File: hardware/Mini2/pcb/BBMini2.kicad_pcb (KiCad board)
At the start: 4 copper layers, 89 x 48 mm, 75 parts, among them J1 Barrel_Jack_Switch, J2 USB_B_Mini, J3 Display, Q1 MBT2222ADW1T1, SW1 SW_SPDT, SW2 SW_Push, SW3 SW_Push, SW4 SW_Push, U1 ESP8266EX, U2 AT25SF081-SSHF-X, U3 AP2112K-3.3, U4 CP2104, U5 MCP3208, U6 LM2576S-5, Y1 ABM8-26.000MHZ-10-1-U-T

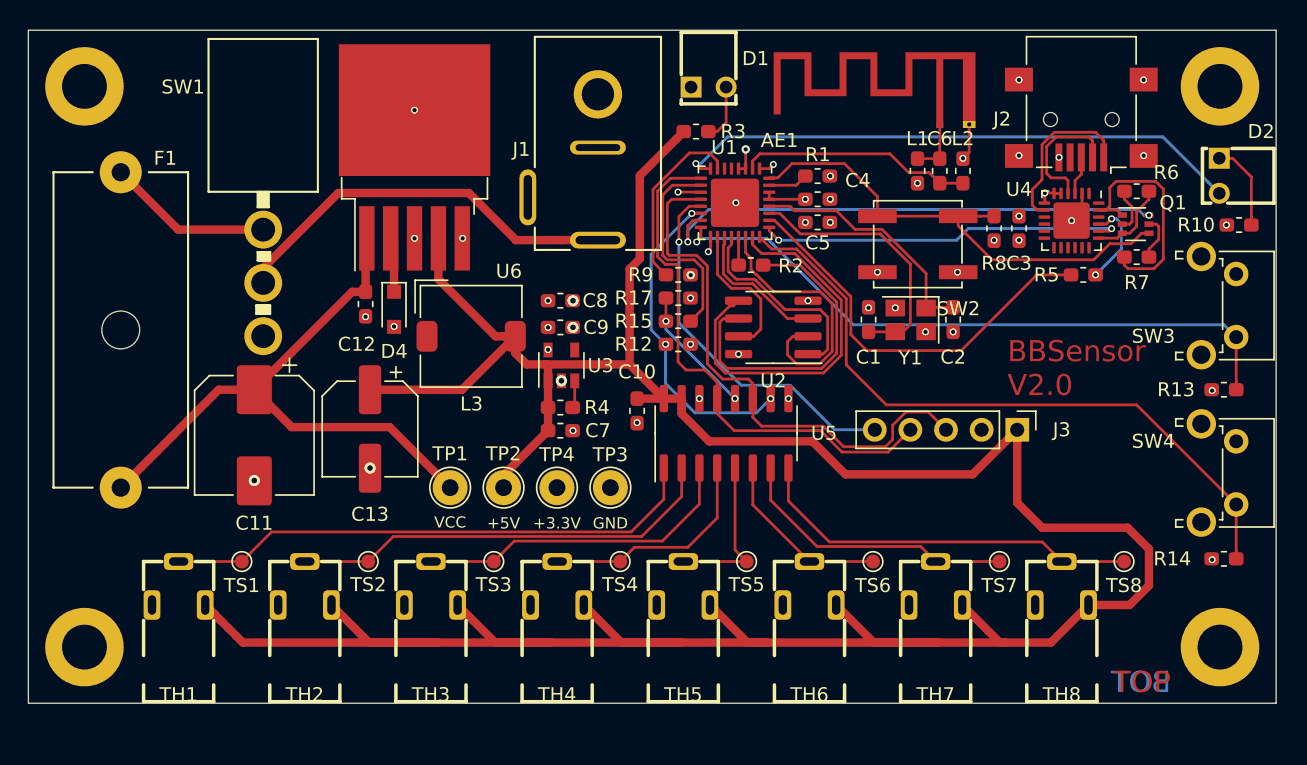
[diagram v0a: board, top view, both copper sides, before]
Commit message: feat: BBMini2 - experimental ESP8266 PCB (SMD)
* shrink pcb, add cad

Issue #23
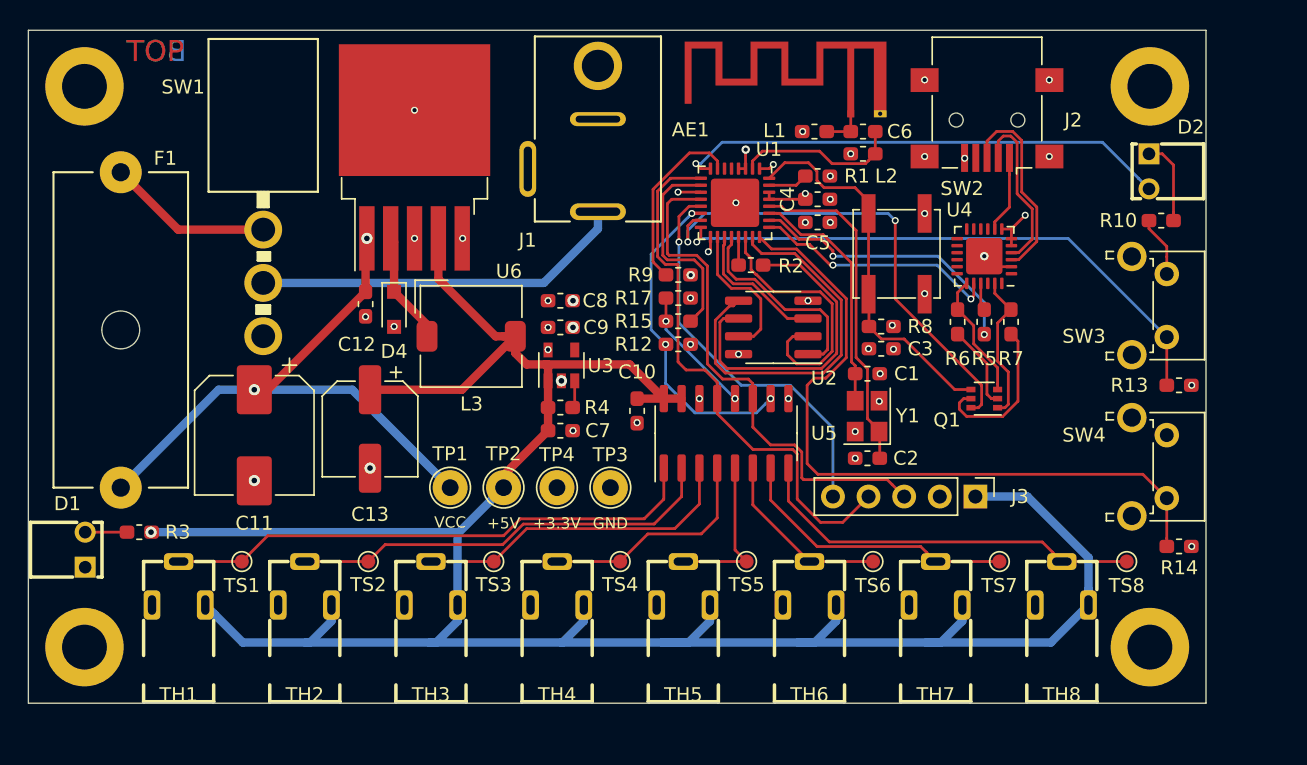
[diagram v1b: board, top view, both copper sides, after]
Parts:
- J1: footprint Collection:CLIFF_DC_SOCKET_2.5 -> Collection:CLIFF_DC_SOCKET_2.5_Short
- moved D1 61.0 mm to (15.1, 52.0), turned to 90 degrees
- moved R3 48.9 mm to (22.9, 50.8), turned to 0 degrees
- moved Q1 16.5 mm to (83.2, 41.3), turned to 180 degrees
- moved R6 15.8 mm to (81.3, 35.8), turned to 270 degrees
- moved C3 13.1 mm to (75.8, 37.7), turned to 180 degrees
- moved C2 11.6 mm to (74.9, 45.5), turned to 0 degrees
- moved R8 10.7 mm to (75.8, 36.1), turned to 0 degrees
- moved R7 10.1 mm to (85.1, 35.8), turned to 270 degrees
- moved L1 7.87 mm to (71.1, 22.2), turned to 180 degrees
- moved R5 7.82 mm to (83.2, 35.8), turned to 270 degrees
- moved Y1 7.53 mm to (74.8, 42.5), turned to 90 degrees
- moved L2 7.23 mm to (74.5, 23.8), turned to 180 degrees
- moved J2 6.73 mm to (83.4, 21.4)
- moved U4 6.72 mm to (83.2, 31.1), turned to 180 degrees
- moved AE1 6.40 mm to (73.7, 21.0)
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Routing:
- net +5V: track 225.8 -> 183.6 mm, vias 0 -> 1
- net Net-(J2-Pad3): track 2.76 -> 14.2 mm
- net /ESP8266EX/GPIO3_RXD: track 29.2 -> 20.3 mm, vias 0 -> 2
- net /ESP8266EX/GPIO1_TXD: track 26.3 -> 17.7 mm
- net Net-(Q1-Pad5): track 3.24 -> 11.2 mm
- net /ESP8266EX/~RST: track 34.9 -> 27.2 mm
- net /Serial/DTR: track 17.0 -> 10.7 mm
- net Net-(J2-Pad1): track 11.8 -> 5.51 mm
- net /ESP8266EX/XTAL_IN: track 17.6 -> 23.9 mm
- net +3V3: track 10.7 -> 16.6 mm, vias 16 -> 15
- net /ESP8266EX/GPIO16: track 41.0 -> 35.5 mm
- net /ESP8266EX/GPIO4: track 46.4 -> 41.1 mm
- net /ESP8266EX/LNA: track 16.6 -> 11.8 mm
- net /Serial/USB_RX: track 6.34 -> 1.98 mm, vias 2 -> 0
- net Net-(D4-Pad1): track 3.91 -> 8.06 mm
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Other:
- board size 89 x 48 mm -> 84 x 48 mm
- board text removed: "BBSensor V2.0"

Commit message: feat: BBMini2 - experimental ESP8266 PCB (SMD)
* redo PCB, add CAD
* make space for Display

Issue #23
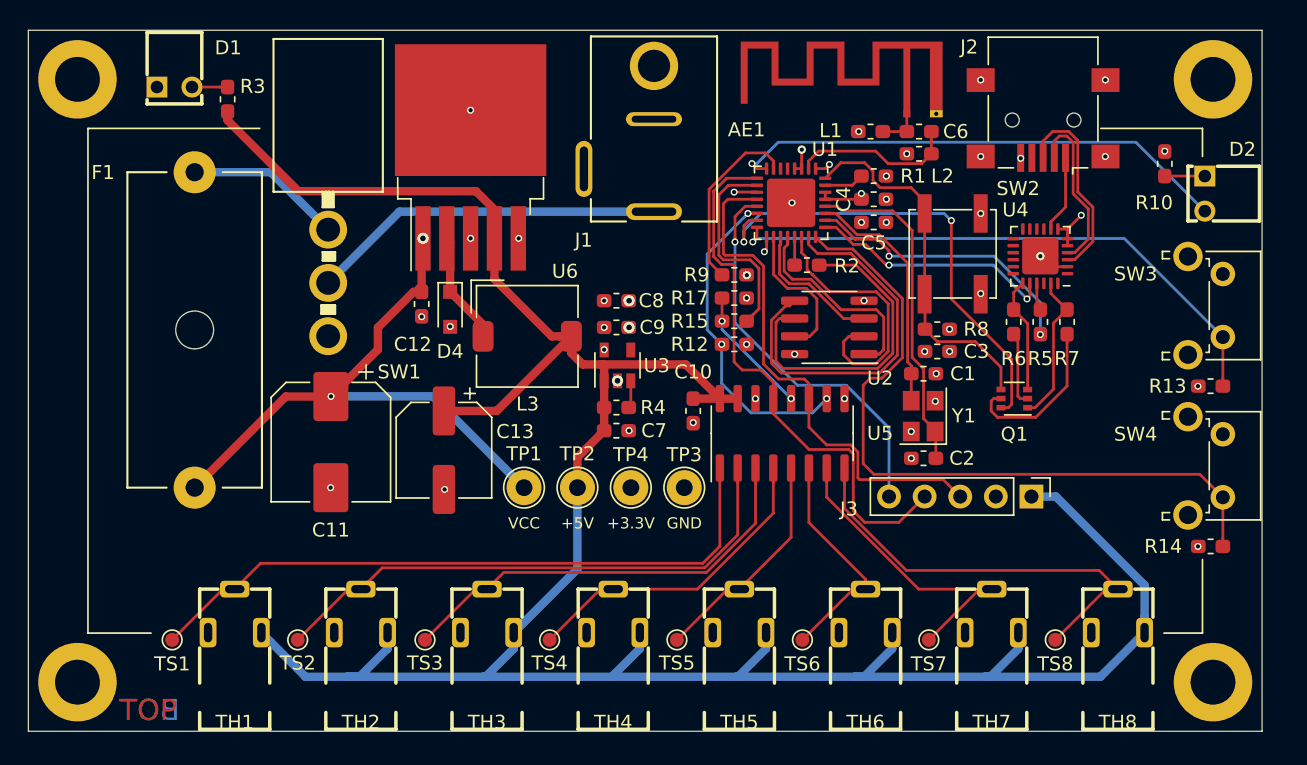
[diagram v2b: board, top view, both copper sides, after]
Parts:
- removed the ~ at (95.0, 19.0)
- removed the ~ at (19.0, 19.0)
- added ~: MountingHole_3.2mm_M3_DIN965_Pad, MountingHole:MountingHole_3.2mm_M3_DIN965_Pad, F.Cu at (18.5, 18.5)
- added ~: MountingHole_3.2mm_M3_DIN965_Pad, MountingHole:MountingHole_3.2mm_M3_DIN965_Pad, F.Cu at (99.5, 18.5)
- moved D1 38.4 mm to (25.4, 15.1), turned to 0 degrees
- moved R3 31.5 mm to (29.2, 19.9), turned to 270 degrees
- moved TS8 7.56 mm to (88.2, 58.5)
- moved TS2 7.52 mm to (34.2, 58.5)
- moved TS4 7.52 mm to (52.2, 58.5)
- moved TS6 7.52 mm to (70.2, 58.5)
- moved TS7 7.52 mm to (79.2, 58.5)
- moved TS5 7.48 mm to (61.3, 58.5)
- moved TS1 7.48 mm to (25.3, 58.5)
- moved TS3 7.44 mm to (43.3, 58.5)
- moved C13 5.48 mm to (44.6, 45.0)
- moved C11 5.48 mm to (36.6, 44.4)
- moved TP4 5.27 mm to (58.0, 47.6)
- moved F1 5.27 mm to (26.9, 47.6)
- moved TP1 5.27 mm to (50.4, 47.6)
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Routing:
- net /Temperature/SIGNAL1: track 38.7 -> 47.4 mm
- net /Temperature/SIGNAL2: track 30.8 -> 39.3 mm
- net /Temperature/SIGNAL3: track 23.4 -> 31.0 mm
- net /Temperature/SIGNAL4: track 16.3 -> 22.9 mm
- net +5V: track 183.6 -> 189.7 mm, vias 1 -> 0
- net /Temperature/SIGNAL5: track 11.5 -> 16.1 mm
- net +3V3: track 16.6 -> 12.2 mm, vias 15 -> 16
- net /Temperature/SIGNAL6: track 12.9 -> 16.3 mm
- net Net-(D2-Pad1): track 6.04 -> 2.86 mm
- net /Temperature/SIGNAL8: track 28.5 -> 30.7 mm
- net /Temperature/SIGNAL7: track 20.4 -> 22.6 mm
- net Net-(J1-Pad1): track 26.7 -> 25.3 mm
- net /ESP8266EX/~RST: track 27.2 -> 26.3 mm
- net /Serial/RTS: track 9.03 -> 8.26 mm
- net /ESP8266EX/GPIO0: track 35.1 -> 34.3 mm
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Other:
- board size 84 x 48 mm -> 88 x 50 mm

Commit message: feat: BBMini2 - experimental ESP8266 PCB (SMD)
* finalize new Case (experimental)

Issue #23
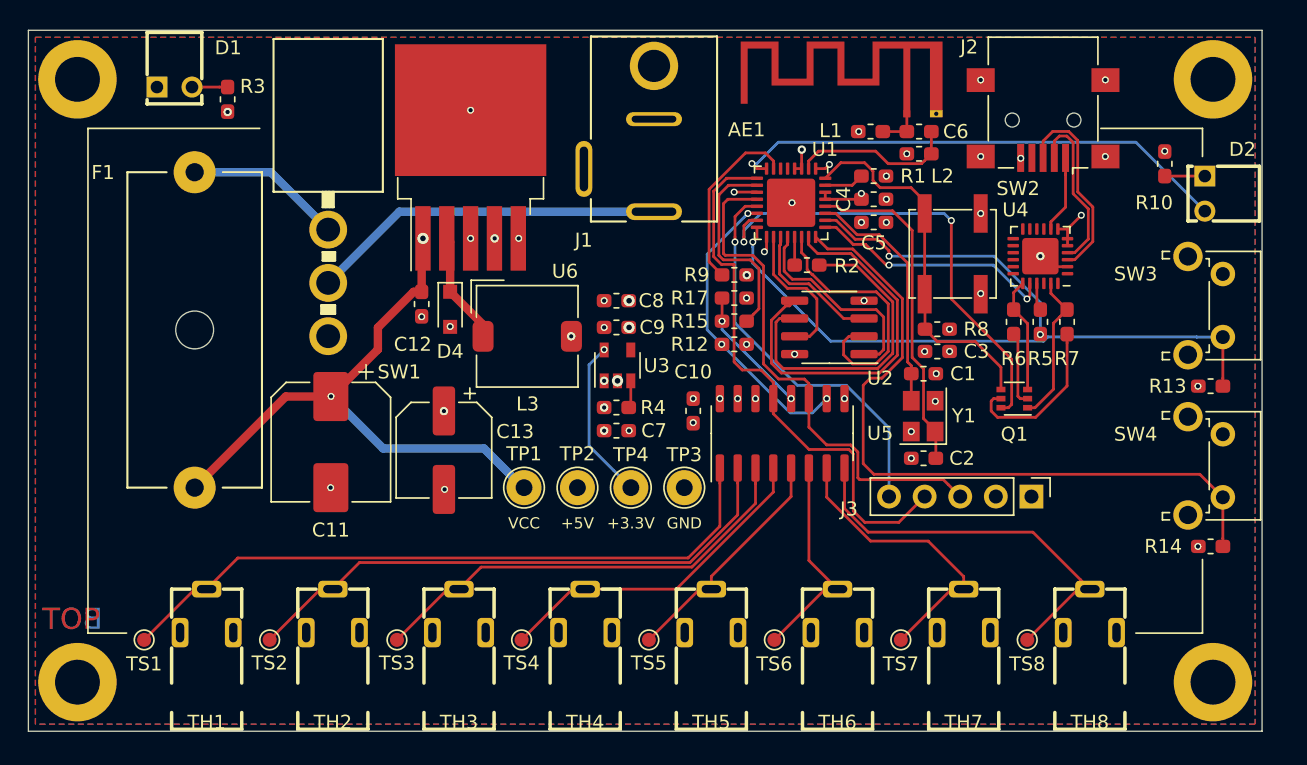
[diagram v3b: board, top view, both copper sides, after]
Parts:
- moved TH1 2.00 mm to (27.7, 64.9)
- moved TH2 2.00 mm to (36.7, 64.9)
- moved TH3 2.00 mm to (45.7, 64.9)
- moved TH4 2.00 mm to (54.7, 64.9)
- moved TH5 2.00 mm to (63.7, 64.9)
- moved TH6 2.00 mm to (72.7, 64.9)
- moved TH7 2.00 mm to (81.7, 64.9)
- moved TH8 2.00 mm to (90.7, 64.9)
- moved TS1 2.00 mm to (23.3, 58.5)
- moved TS2 2.00 mm to (32.2, 58.5)
- moved TS3 2.00 mm to (41.3, 58.5)
- moved TS4 2.00 mm to (50.2, 58.5)
- moved TS5 2.00 mm to (59.3, 58.5)
- moved TS6 2.00 mm to (68.2, 58.5)
- moved TS7 2.00 mm to (77.2, 58.5)
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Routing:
- net +5V: track 189.7 -> 0.00 mm, vias 0 -> 10
- net +3V3: track 12.2 -> 23.8 mm
- net /Temperature/SIGNAL8: track 30.7 -> 28.7 mm
- net /ESP8266EX/CS1: track 23.2 -> 21.6 mm
- net /Temperature/SIGNAL7: track 22.6 -> 21.1 mm
- net /Temperature/SIGNAL1: track 47.4 -> 48.6 mm
- net /Temperature/SIGNAL3: track 31.0 -> 32.1 mm
- net /Temperature/SIGNAL2: track 39.3 -> 40.4 mm
- net /Temperature/SIGNAL4: track 22.9 -> 24.0 mm
- net /ESP8266EX/GPIO4: track 41.2 -> 42.2 mm
- net /Temperature/SIGNAL5: track 16.1 -> 17.0 mm
- net /Temperature/SIGNAL6: track 16.3 -> 15.5 mm
- added copper zone on In1.Cu, net +5V
- added copper zone on B.Cu, net GND
- added copper zone on F.Cu, net GND

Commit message: feat: BBMini2 - experimental ESP8266 PCB (SMD)
* add Display to Mini2

Issue #23
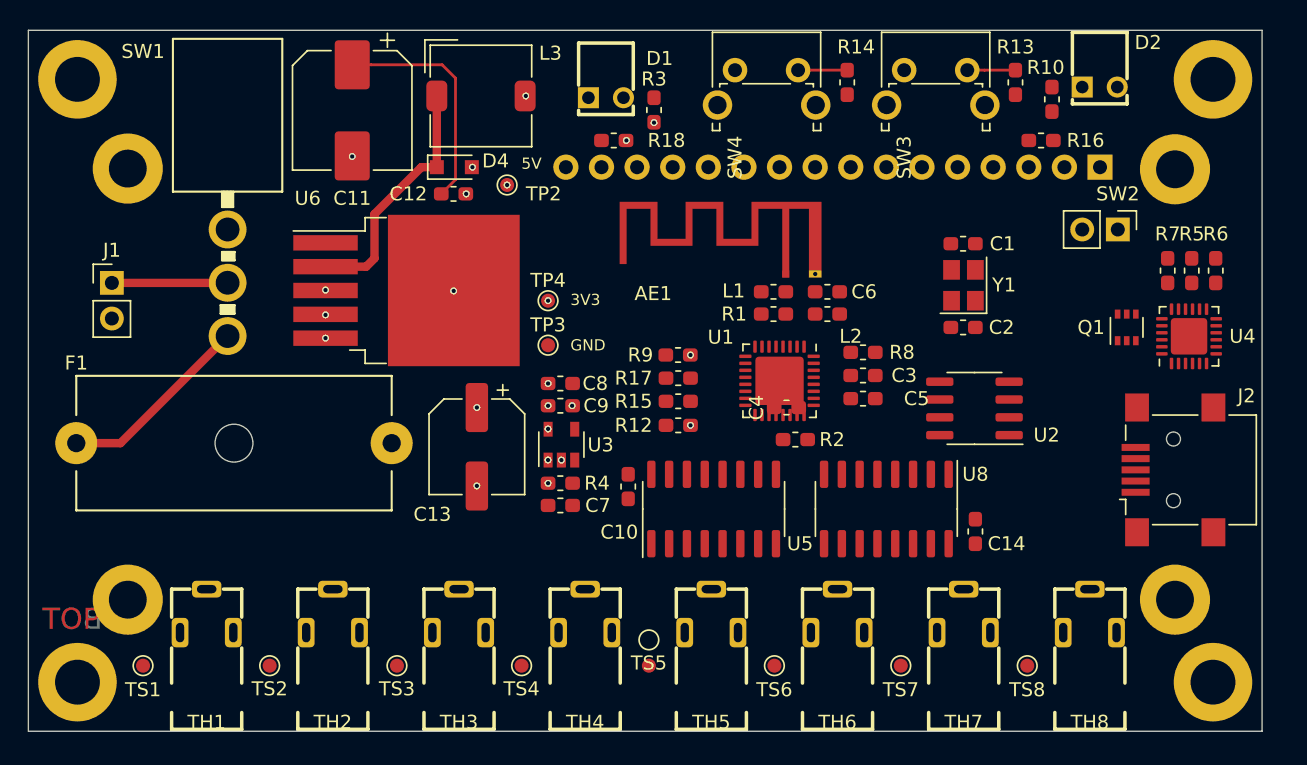
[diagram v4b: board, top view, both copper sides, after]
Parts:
- removed J3: Display, Connector_PinHeader_2.54mm:PinHeader_1x05_P2.54mm_Vertical
- removed TP1: TestPoint, TestPoint:TestPoint_THTPad_D2.5mm_Drill1.2mm
- added C14: 100n, Capacitor_SMD:C_0603_1608Metric_Pad1.05x0.95mm_HandSolder, F.Cu at (82.5, 50.8)
- added R16: 2k, Resistor_SMD:R_0603_1608Metric_Pad1.05x0.95mm_HandSolder, F.Cu at (87.2, 22.9)
- added R18: 220, Resistor_SMD:R_0603_1608Metric_Pad1.05x0.95mm_HandSolder, F.Cu at (56.8, 22.9)
- added U7: HD44780, Collection:HD44780_LCD_2x16, B.Cu at (59.4, 40.3)
- added U8: 74HC595, Package_SO:SOIC-16_3.9x9.9mm_P1.27mm, F.Cu at (76.2, 49.1)
- J1: value Barrel_Jack_Switch -> Conn_01x02; footprint Collection:CLIFF_DC_SOCKET_2.5_Short -> Connector_PinHeader_2.54mm:PinHeader_1x02_P2.54mm_Vertical
- SW2: footprint Button_Switch_SMD:SW_SPST_EVPBF -> Connector_PinHeader_2.54mm:PinHeader_1x02_P2.54mm_Vertical
- TP2, TP3, TP4: footprint TestPoint:TestPoint_THTPad_D2.5mm_Drill1.2mm -> TestPoint:TestPoint_Pad_D1.0mm
- moved SW4 43.4 mm to (65.4, 17.8), turned to 0 degrees
- moved R14 42.0 mm to (73.4, 18.7), turned to 270 degrees
- moved J1 39.0 mm to (21.0, 33.0), turned to 0 degrees
- moved D1 30.8 mm to (56.2, 15.8)
- moved R3 30.4 mm to (59.6, 20.7)
- moved SW3 27.0 mm to (77.5, 17.8), turned to 0 degrees
- moved J2 26.6 mm to (96.7, 46.4), turned to 90 degrees
- moved R13 25.8 mm to (85.4, 18.7), turned to 270 degrees
- moved C11 23.7 mm to (38.1, 20.7)
- moved TP2 22.2 mm to (49.1, 26.0)
- moved L3 17.5 mm to (47.3, 19.7)
- moved D2 16.3 mm to (91.4, 15.1), turned to 0 degrees
- moved C4 16.1 mm to (69.1, 41.9)
- moved R6 14.9 mm to (99.7, 32.1), turned to 90 degrees
- moved TP4 14.6 mm to (52.1, 34.3)
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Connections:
- net VCC renamed Net-(C11-Pad1)
- SW1 pad 1: Net-(SW1-Pad1) -> Net-(F1-Pad2)
- SW1 pad 3: Net-(F1-Pad2) -> Net-(SW1-Pad3)
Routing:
- net /Temperature/SIGNAL1: track 48.6 -> 0.00 mm
- net /ESP8266EX/GPIO5: track 51.6 -> 3.50 mm
- net /Temperature/SIGNAL2: track 40.4 -> 0.00 mm
- net /ESP8266EX/SCLK: track 39.6 -> 0.00 mm
- net /ESP8266EX/GPIO4: track 42.2 -> 3.44 mm, vias 1 -> 0
- net /ESP8266EX/MOSI: track 37.1 -> 0.00 mm
- net /ESP8266EX/GPIO16: track 36.2 -> 0.00 mm, vias 1 -> 0
- net /ESP8266EX/GPIO0: track 34.3 -> 0.00 mm, vias 2 -> 0
- net /Temperature/SIGNAL3: track 32.1 -> 0.00 mm
- net /Temperature/SIGNAL8: track 28.7 -> 0.00 mm
- net /ESP8266EX/GPIO15: track 28.4 -> 0.00 mm, vias 1 -> 0
- net /ESP8266EX/SDIO_DATA_1: track 27.5 -> 0.00 mm
- net Net-(C11-Pad1): track 43.2 -> 16.4 mm, vias 2 -> 0
- net /ESP8266EX/~RST: track 26.3 -> 0.00 mm
- net /Temperature/SIGNAL4: track 24.0 -> 0.00 mm
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- removed copper zone on B.Cu, net GND
- removed copper zone on F.Cu, net GND
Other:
- board text added: "3V3"
- board text added: "5V"
- board text removed: "+3.3V"
- board text removed: "+5V"
- board text removed: "VCC"

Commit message: feat: BBMini2 - experimental ESP8266 PCB (SMD)
* add display to pcb

Issue #23
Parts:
- added C14: 100n, Capacitor_SMD:C_0603_1608Metric_Pad1.05x0.95mm_HandSolder, F.Cu at (99.9, 39.1)
- moved C13 23.3 mm to (68.6, 32.1)
- moved U8 23.3 mm to (62.2, 30.5)
- moved C10 15.4 mm to (87.4, 33.6)
- moved L2 15.4 mm to (83.6, 33.6)
- moved L3 15.4 mm to (87.4, 35.2)
- moved AE1 15.4 mm to (84.5, 32.4)
- moved C11 15.3 mm to (87.2, 44.5), turned to 0 degrees
- moved R8 12.3 mm to (79.6, 39.8), turned to 0 degrees
- moved C8 10.9 mm to (79.6, 44.6)
- moved Y1 9.92 mm to (87.2, 41.4), turned to 270 degrees
- moved U2 7.90 mm to (78.7, 48.9)
- moved R16 7.74 mm to (92.5, 34.9), turned to 180 degrees
- moved TP1 7.01 mm to (52.7, 30.5)
- moved C12 6.01 mm to (87.2, 38.5), turned to 180 degrees
- moved R6 5.93 mm to (67.1, 41.6)
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- renumbered C11 to C1, C6 to C10, C1 to C11, C2 to C12, C14 to C13, C10 to C15, C12 to C2, C13 to C3, C7 to C4, C8 to C5, C9 to C6, C3 to C7, C4 to C8, C5 to C9, D4 to D1, D1 to D2, D2 to D3, L3 to L1, L1 to L2, L2 to L3, R3 to R1, R14 to R10, R15 to R11, R17 to R12, R16 to R13, R18 to R14, R5 to R15, R6 to R16, R7 to R17, R4 to R2, R8 to R3, R9 to R4, R10 to R5, R12 to R6, R2 to R7, R1 to R8, R13 to R9, TP3 to TP1, TP4 to TP3
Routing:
- net /ESP8266EX/GPIO16: track 0.00 -> 48.6 mm, vias 0 -> 2
- net /Temperature/SIGNAL1: track 0.00 -> 42.1 mm, vias 0 -> 1
- net /ESP8266EX/GPIO0: track 0.00 -> 40.8 mm
- net /ESP8266EX/GPIO4: track 3.44 -> 40.0 mm, vias 0 -> 2
- net /Temperature/SIGNAL2: track 0.00 -> 34.2 mm, vias 0 -> 1
- net /ESP8266EX/GPIO3_RXD: track 0.00 -> 33.8 mm, vias 0 -> 2
- net /Temperature/SIGNAL8: track 0.00 -> 32.7 mm, vias 0 -> 1
- net /ESP8266EX/GPIO1_TXD: track 0.00 -> 32.6 mm, vias 0 -> 2
- net /ESP8266EX/RS: track 0.00 -> 30.1 mm
- net /ESP8266EX/MOSI: track 0.00 -> 30.1 mm
- net /ESP8266EX/SCLK: track 0.00 -> 28.1 mm, vias 0 -> 2
- net /ESP8266EX/GPIO5: track 3.50 -> 31.5 mm, vias 0 -> 2
- net /Temperature/SIGNAL3: track 0.00 -> 26.4 mm, vias 0 -> 1
- net /Temperature/SIGNAL7: track 0.00 -> 26.1 mm, vias 0 -> 1
- net /ESP8266EX/~RST: track 0.00 -> 24.9 mm
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
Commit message: feat: BBMini2 - experimental ESP8266 PCB (SMD)
* redo CAD, switch LEDs

Issue #23
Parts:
- D2, D3: footprint VCC:5600F -> LED_THT:LED_D3.0mm; moved to B.Cu
- moved D3 4.05 mm to (90.8, 19.1)
- moved D2 3.61 mm to (54.6, 19.1)
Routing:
- net /ESP8266EX/GPIO16: track 48.6 -> 50.1 mm
- net Net-(D3-Pad1): track 2.40 -> 3.03 mm
- net Net-(D2-Pad2): track 2.18 -> 2.79 mm
